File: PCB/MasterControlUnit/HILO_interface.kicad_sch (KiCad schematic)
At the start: 0 parts

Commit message: Backup version
before to remove the SPI dedicated to the interative mode communication. In these modality the SPI is used by the STM32 to send
data stream the ESP32. Unfortunately the ESP32 can use just two SPI external ports
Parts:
- added U16: ESP32-DevKitC, PCM_Espressif:ESP32-DevKitC, symbol ESP32:ESP32-DevKitC
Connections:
- new net +5V: U16.19 (5V)
- new net CS to ESP32: U16.11 (ADC2_CH7/GPIO27)
- new net GND: U16.14 (GND), U16.32 (GND), U16.38 (GND)
- new net ISRAM ADDR 0: U16.33 (GPIO21)
- new net MISO from ESP32: U16.13 (MTDI/GPIO12/ADC2_CH5)
- new net MISO from ISRAM: U16.31 (GPIO19)
- new net MISO from OSRAM: U16.8 (32K_XN/GPIO33/ADC1_CH5)
- new net MOSI to ESP32: U16.15 (MTCK/GPIO13/ADC2_CH4)
- new net MOSI to ISRAM: U16.37 (GPIO23)
- new net MOSI to OSRAM: U16.28 (GPIO17)
- new net OSRAM ADDR 0: U16.26 (ADC2_CH0/GPIO4)
- new net OSRAM ADDR 1: U16.23 (MTDO/GPIO15/ADC2_CH3)
- new net OSRAM ADDR 2: U16.24 (ADC2_CH2/GPIO2)
- new net OSRAM B-EN: U16.36 (GPIO22), U16.7 (32K_XP/GPIO32/ADC1_CH4)
- new net SCL/SCK to ESP32: U16.12 (MTMS/GPIO14/ADC2_CH6)
- new net SCL/SCK to ISRAM: U16.30 (GPIO18)
- new net SCL/SCK to OSRAM: U16.27 (GPIO16)
- no-connect marks 0 -> 2
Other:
- title: (none) -> HILO's Interface System

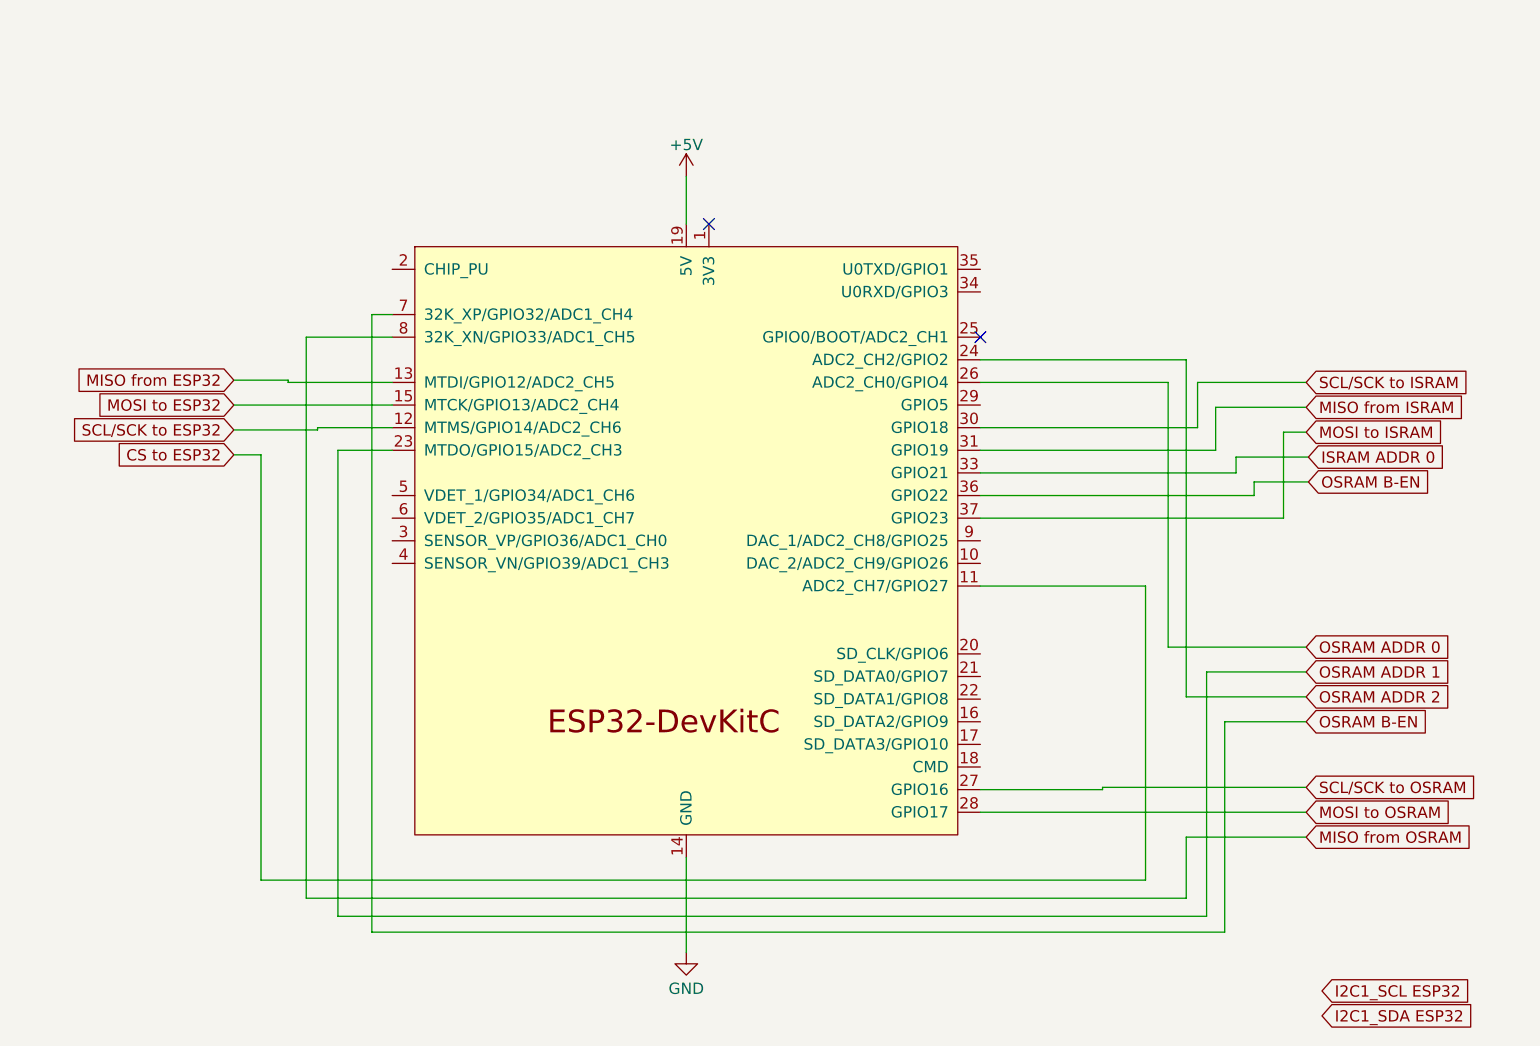
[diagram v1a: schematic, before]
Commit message: Important achitectural change (or fix)
Because ESP32 provides just two SPI ports, the original idea to use a dedicated SPI from STM32 to ESP32 cannot be implemented.
That SPI port was meant to be used in the interactive mode to send data from the STM32 to the ESP32.
The new idea is to use the SPI bus used to read/write the 64MB SRAM. The two MCU already shared that bus
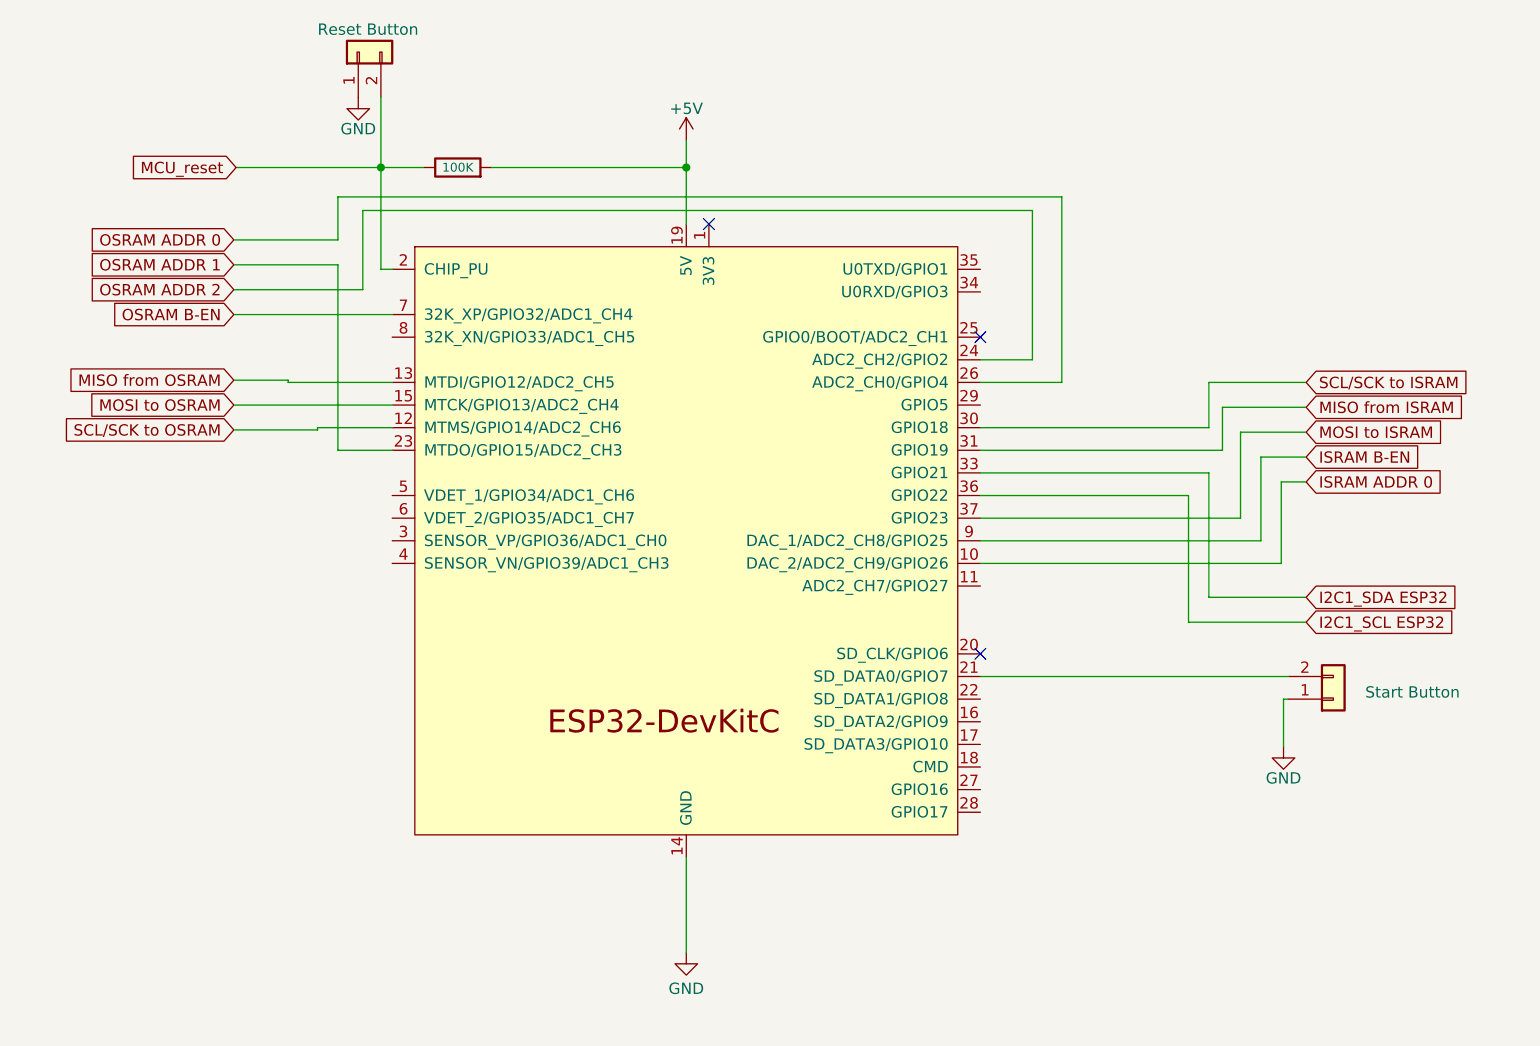
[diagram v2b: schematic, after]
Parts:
- added J1: Reset Button, symbol Connector_Generic:Conn_01x02
- added J2: Start Button, symbol Connector_Generic:Conn_01x02
- added R1: 100K, symbol Device:R
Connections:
- net MISO from ESP32 is gone; now on net MISO from OSRAM: U16.13 (MTDI/GPIO12/ADC2_CH5)
- net MOSI to ESP32 is gone; now on net MOSI to OSRAM: U16.15 (MTCK/GPIO13/ADC2_CH4)
- net SCL/SCK to ESP32 is gone; now on net SCL/SCK to OSRAM: U16.12 (MTMS/GPIO14/ADC2_CH6)
- net +5V: now also R1.2
- net GND: now also J1.1 (Pin_1), J2.1 (Pin_1)
- net I2C1_SCL ESP32: now also U16.36 (GPIO22)
- net I2C1_SDA ESP32: now also U16.33 (GPIO21)
- net ISRAM ADDR 0: now also U16.10 (DAC_2/ADC2_CH9/GPIO26); no longer U16.33 (GPIO21)
- net MISO from OSRAM: no longer U16.8 (32K_XN/GPIO33/ADC1_CH5)
- net MOSI to OSRAM: no longer U16.28 (GPIO17)
- net OSRAM B-EN: no longer U16.36 (GPIO22)
- net SCL/SCK to OSRAM: no longer U16.27 (GPIO16)
- net MCU_reset: now reaches U16.2 (CHIP_PU)
- net MCU_reset: now also J1.2 (Pin_2), R1.1
- net at U16.21 (SD_DATA0/GPIO7): now also J2.2 (Pin_2)
- net ISRAM B-EN: now reaches U16.9 (DAC_1/ADC2_CH8/GPIO25)
- net CS to ESP32: no longer names the net of U16.11 (ADC2_CH7/GPIO27)
- no-connect marks 2 -> 3

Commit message: Components footprints configured
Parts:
- J1, J2: footprint (none) -> Connector_PinHeader_2.54mm:PinHeader_1x02_P2.54mm_Vertical
- R1: footprint (none) -> Resistor_SMD:R_1206_3216Metric
- U16: footprint PCM_Espressif:ESP32-DevKitC -> Espressif:ESP32-DevKitC
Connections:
- net RS232-RX: now reaches U16.34 (U0RXD/GPIO3)
- net RS232-TX: now reaches U16.35 (U0TXD/GPIO1)
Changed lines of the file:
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@@
+	(wire
+		(pts
+			(xy 185.674 66.548) (xy 185.674 66.04)
+		)
+		(stroke
+			(width 0)
+			(type default)
+		)
+	)
 	(wire
 		(pts
@@
 	(wire
 		(pts
+			(xy 174.498 63.5) (xy 211.074 63.5)
+		)
+		(stroke
+			(width 0)
+			(type default)
+		)
+	)
+	(wire
+		(pts
 			(xy 197.866 103.124) (xy 197.866 88.9)
 		)
@@
 	(wire
 		(pts
+			(xy 211.074 66.548) (xy 185.674 66.548)
+		)
+		(stroke
+			(width 0)
+			(type default)
+		)
+	)
+	(wire
+		(pts
 			(xy 205.994 84.582) (xy 205.994 93.98)
 		)
@@
 	(wire
 		(pts
+			(xy 185.674 66.04) (xy 174.498 66.04)
+		)
+		(stroke
+			(width 0)
+			(type default)
+		)
+	)
+	(wire
+		(pts
 			(xy 200.152 100.33) (xy 200.152 86.36)
 		)
@@
 		)
 	)
+	(global_label "RS232-TX"
+		(shape input)
+		(at 211.074 63.5 0)
+		(fields_autoplaced yes)
+		(effects
+			(font
+				(size 1.27 1.27)
+			)
+			(justify left)
+		)
+		(property "Intersheetrefs" "${INTERSHEET_REFS}"
+			(at 223.9167 63.5 0)
+			(effects
+				(font
+					(size 1.27 1.27)
+				)
+				(justify left)
+				(hide yes)
+			)
+		)
+	)
 	(global_label "ISRAM B-EN"
 		(shape input)
@@
 				)
 				(justify right)
+				(hide yes)
+			)
+		)
+	)
+	(global_label "RS232-RX"
+		(shape input)
+		(at 211.074 66.548 0)
+		(fields_autoplaced yes)
+		(effects
+			(font
+				(size 1.27 1.27)
+			)
+			(justify left)
+		)
+		(property "Intersheetrefs" "${INTERSHEET_REFS}"
+			(at 224.2191 66.548 0)
+			(effects
+				(font
+					(size 1.27 1.27)
+				)
+				(justify left)
 				(hide yes)
 			)
@@
 			)
 		)
-		(property "Footprint" "PCM_Espressif:ESP32-DevKitC"
+		(property "Footprint" "Espressif:ESP32-DevKitC"
 			(at 141.478 137.16 0)
 			(effects
@@
 			)
 		)
-		(property "Footprint" ""
+		(property "Footprint" "Resistor_SMD:R_1206_3216Metric"
 			(at 115.824 53.848 90)
 			(effects
@@
 			)
 		)
-		(property "Footprint" ""
+		(property "Footprint" "Connector_PinHeader_2.54mm:PinHeader_1x02_P2.54mm_Vertical"
 			(at 104.648 39.116 0)
 			(effects
@@
 			)
 		)
-		(property "Footprint" ""
+		(property "Footprint" "Connector_PinHeader_2.54mm:PinHeader_1x02_P2.54mm_Vertical"
 			(at 214.122 111.76 0)
 			(effects
